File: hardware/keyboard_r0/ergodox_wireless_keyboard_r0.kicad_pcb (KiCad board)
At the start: 2 copper layers, 180.1 x 154.6 mm, 178 parts

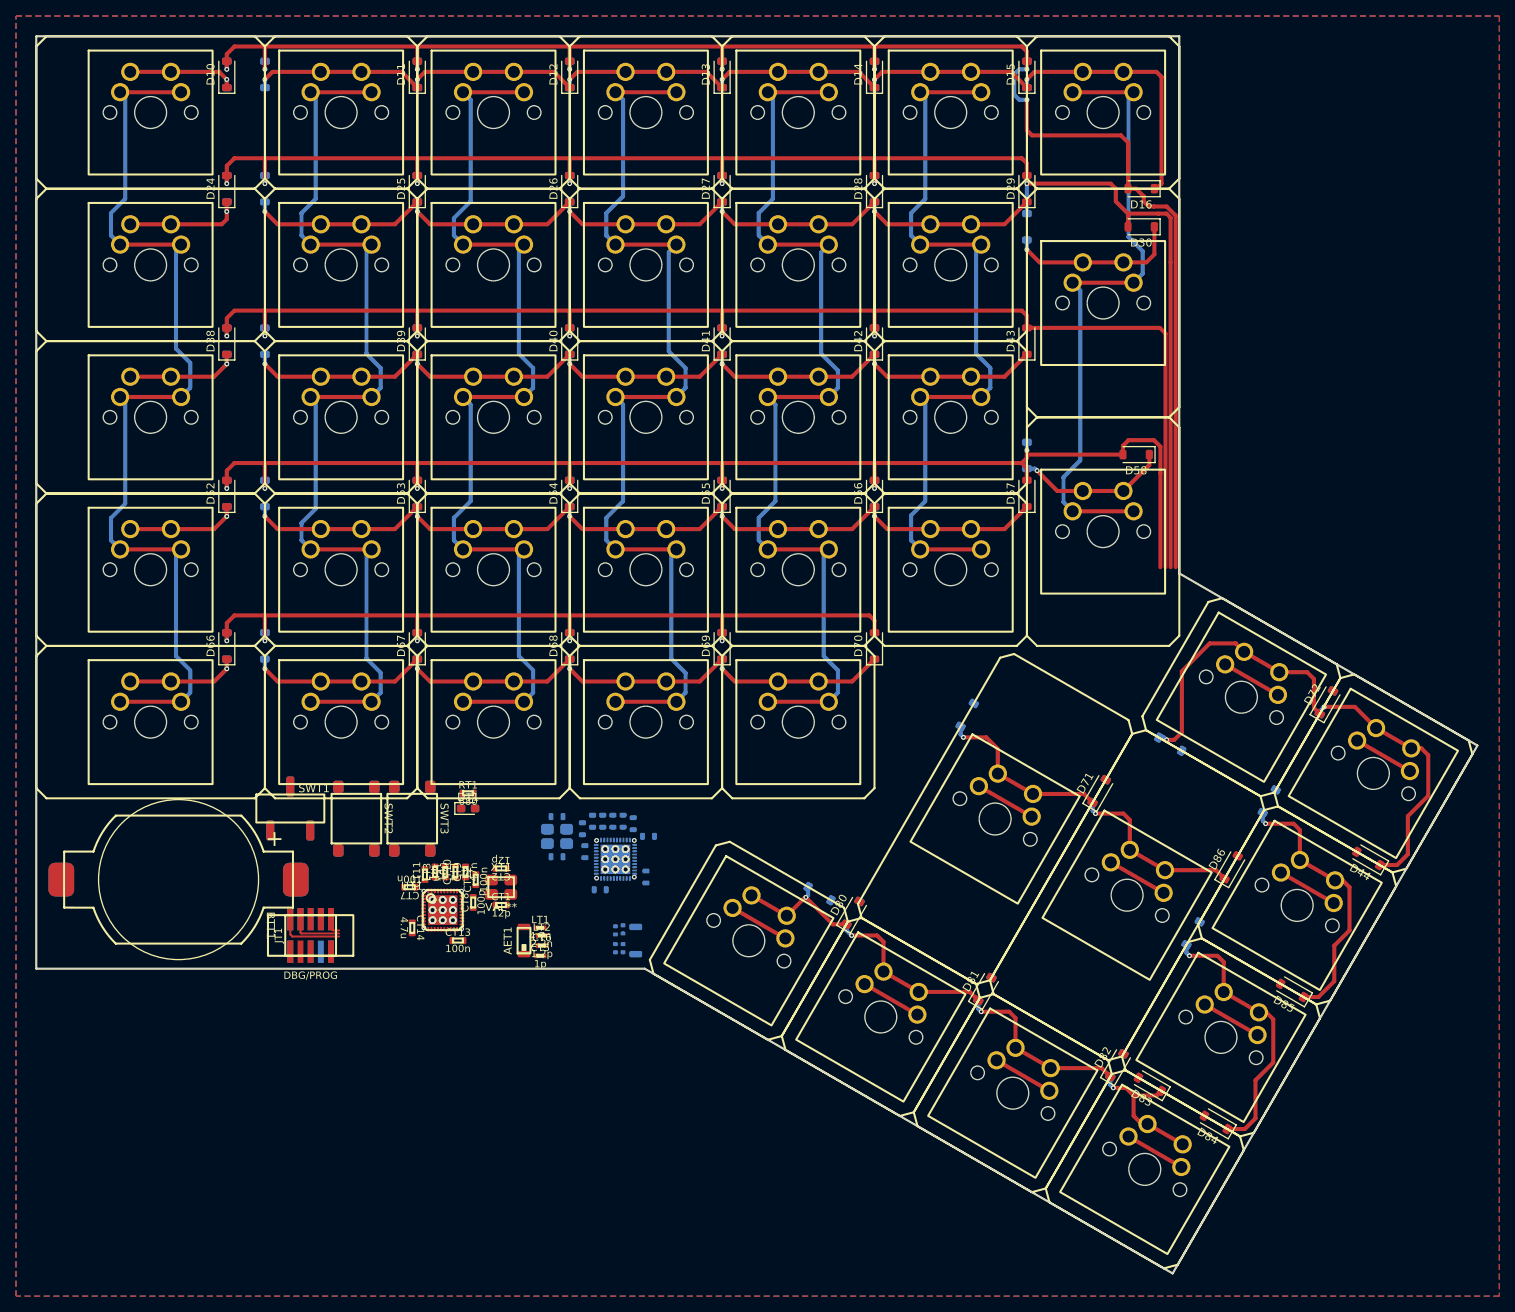
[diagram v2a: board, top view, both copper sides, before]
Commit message: Begin to route traces around the microcontroller.
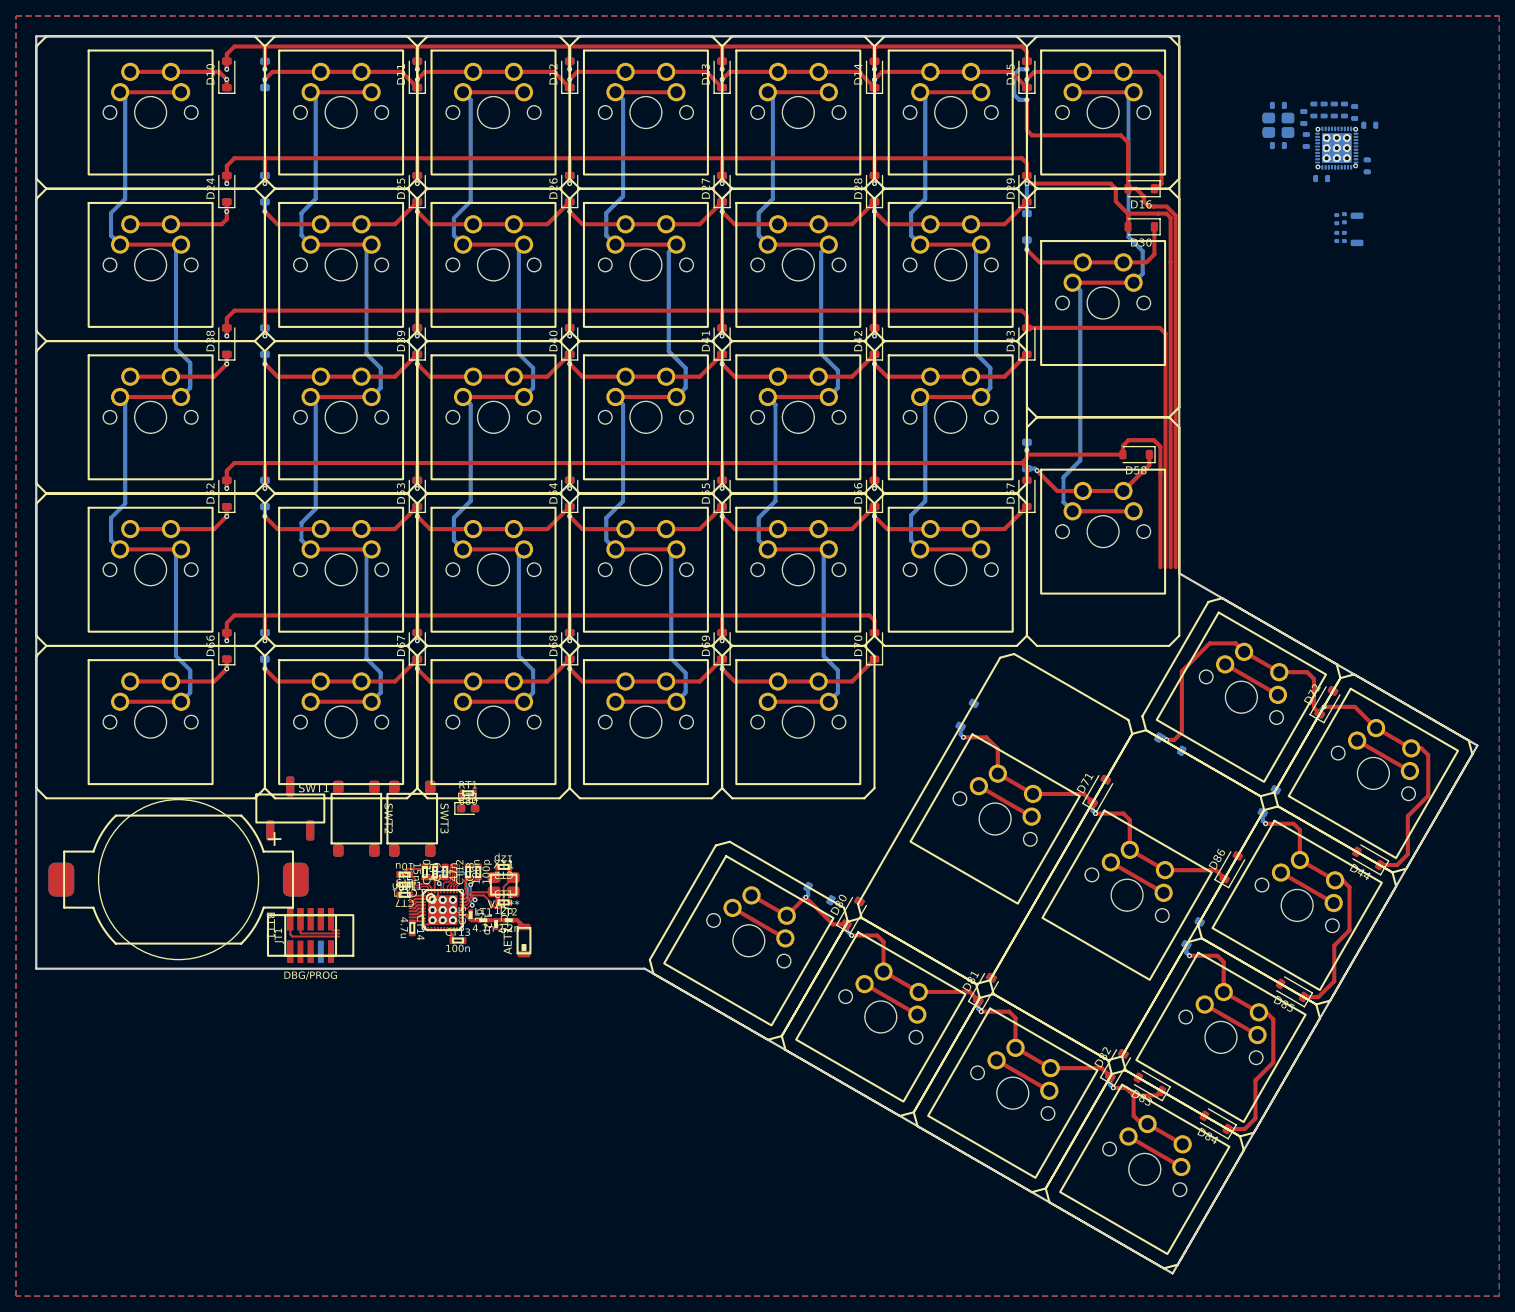
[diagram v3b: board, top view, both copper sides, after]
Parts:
- moved CB10 126.6 mm to (183.8, 32.1)
- moved CB11 126.6 mm to (187.6, 32.4)
- moved CB7 126.6 mm to (189.5, 34.0)
- moved CB8 126.6 mm to (181.6, 35.9)
- moved CB1 126.6 mm to (178.1, 36.5)
- moved CB12 126.6 mm to (181.3, 33.0)
- moved CB14 126.6 mm to (189.2, 39.1)
- moved CB2 126.6 mm to (178.1, 31.5)
- moved CB5 126.6 mm to (185.4, 45.7)
- moved CB6 126.6 mm to (186.4, 45.6)
- moved CB9 126.6 mm to (182.6, 32.1)
- moved LB1 126.6 mm to (186.4, 47.9)
- moved LB2 126.6 mm to (185.4, 47.9)
- moved LB3 126.6 mm to (186.4, 32.1)
- moved LB4 126.6 mm to (185.1, 32.1)
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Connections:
- UB1 pad 17: unconnected-(UB1-P0.20-Pad17) -> /Bottom Microcontroller/COL5
- UB1 pad 22: /Bottom Microcontroller/COL5 -> unconnected-(UB1-P0.16-Pad22)
- UB1 pad 23: /Bottom Microcontroller/COL6 -> unconnected-(UB1-P0.17-Pad23)
- UB1 pad 34: unconnected-(UB1-P0.28-Pad34) -> /Bottom Microcontroller/COL6
- UT1 pad 17: unconnected-(UT1-P0.20-Pad17) -> /Bottom Microcontroller/COL5
- UT1 pad 22: /Bottom Microcontroller/COL5 -> unconnected-(UT1-P0.16-Pad22)
- UT1 pad 23: /Bottom Microcontroller/COL6 -> unconnected-(UT1-P0.17-Pad23)
- UT1 pad 34: unconnected-(UT1-P0.28-Pad34) -> /Bottom Microcontroller/COL6
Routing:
- net Net-(UT1-DEC4): track 0.00 -> 14.5 mm, vias 0 -> 2
- net Net-(UT1-XC1): track 0.00 -> 11.9 mm
- net /Top Microcontroller/3V0: track 0.00 -> 8.71 mm
- net GND: track 0.00 -> 8.28 mm
- net Net-(UT1-XC2): track 0.00 -> 5.80 mm
- net Net-(UT1-DEC3): track 0.00 -> 5.36 mm, vias 0 -> 2
- net Net-(UT1-DCC): track 0.00 -> 4.29 mm
- net /Bottom Microcontroller/ROW3: track 162.8 -> 166.8 mm
- net Net-(LT3-Pad2): track 0.00 -> 3.86 mm
- net /Bottom Microcontroller/COL6: track 101.3 -> 104.9 mm
- net Net-(UT1-P0.30): track 0.00 -> 3.53 mm
- net Net-(DT1-A): track 0.00 -> 3.48 mm
- net /Bottom Microcontroller/COL2: track 128.3 -> 131.8 mm
- net Net-(UT1-ANT): track 0.00 -> 2.45 mm
- net Net-(CT6-Pad1): track 0.00 -> 2.16 mm
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
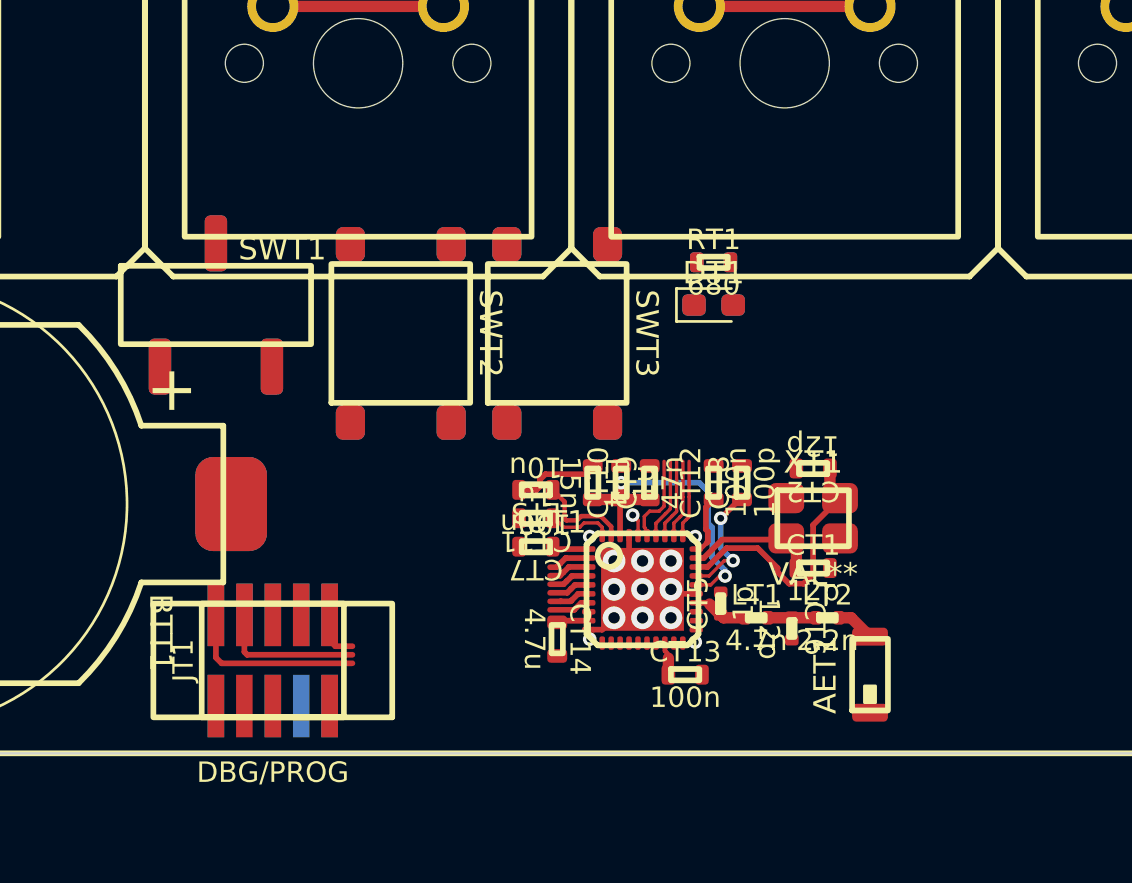
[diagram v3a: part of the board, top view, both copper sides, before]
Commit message: Finish routing most of the top micro circuits
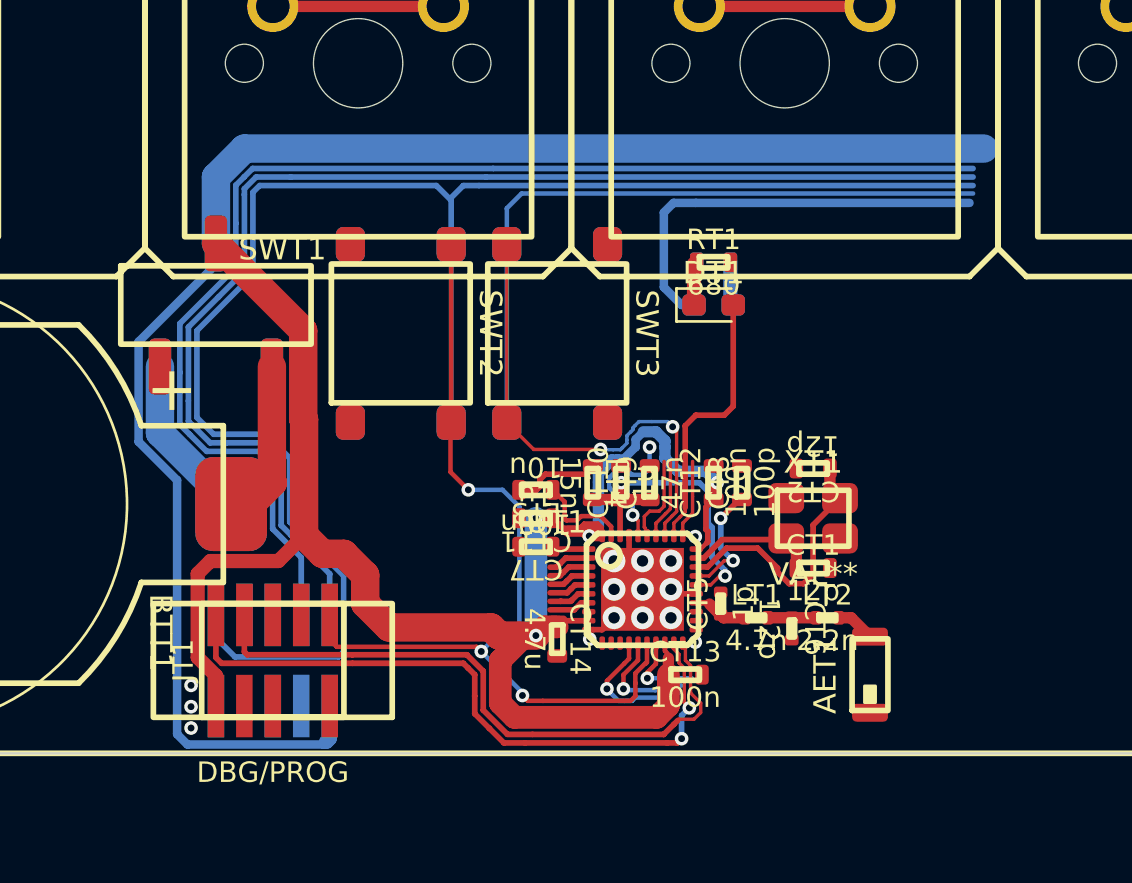
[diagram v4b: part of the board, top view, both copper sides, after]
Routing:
- net /Bottom Microcontroller/~{RESET}: track 0.00 -> 75.6 mm
- net /Top Microcontroller/3V0: track 8.71 -> 83.6 mm, vias 0 -> 4
- net /Bottom Microcontroller/3V0: track 0.00 -> 70.7 mm
- net /Bottom Microcontroller/SWDCLK: track 0.00 -> 57.1 mm
- net /Bottom Microcontroller/SWDIO: track 0.00 -> 56.8 mm
- net /Top Microcontroller/~{RESET}: track 2.27 -> 40.1 mm, vias 0 -> 3
- net Net-(UB1-P0.30): track 0.00 -> 30.7 mm
- net /Top Microcontroller/SWDIO: track 8.11 -> 30.1 mm, vias 0 -> 2
- net /Top Microcontroller/SWDCLK: track 6.53 -> 28.4 mm
- net Net-(DB1-A): track 0.00 -> 18.8 mm
- net Net-(UT1-P0.30): track 3.53 -> 21.9 mm, vias 0 -> 2
- net Net-(DT1-A): track 3.48 -> 12.1 mm
- net Net-(BTT1-+): track 0.00 -> 7.46 mm
- net Net-(BTB1-+): track 0.00 -> 7.46 mm
- net /Bottom Microcontroller/COL3: track 128.6 -> 134.6 mm, vias 0 -> 1
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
